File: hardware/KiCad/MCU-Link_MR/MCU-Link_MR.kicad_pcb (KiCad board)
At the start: 2 copper layers, 57.9 x 39.9 mm, 108 parts, among them J1 Pixhawk Debug Full (1x10 JST-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, J11 JST-GH_BM06B, J2 Pixhawk_Debug_Mini (1x06 JST-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, J3 Jumper_2_Open, J4 Jumper_2_Open, J5 Jumper_2_Open, J6 Conn_02x05_Odd_Even, J8 DCD-LZ_Debug (1x07 JST-GHS), J9 USB4110-GF-A_REVB, SW1 KMR221GLFS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

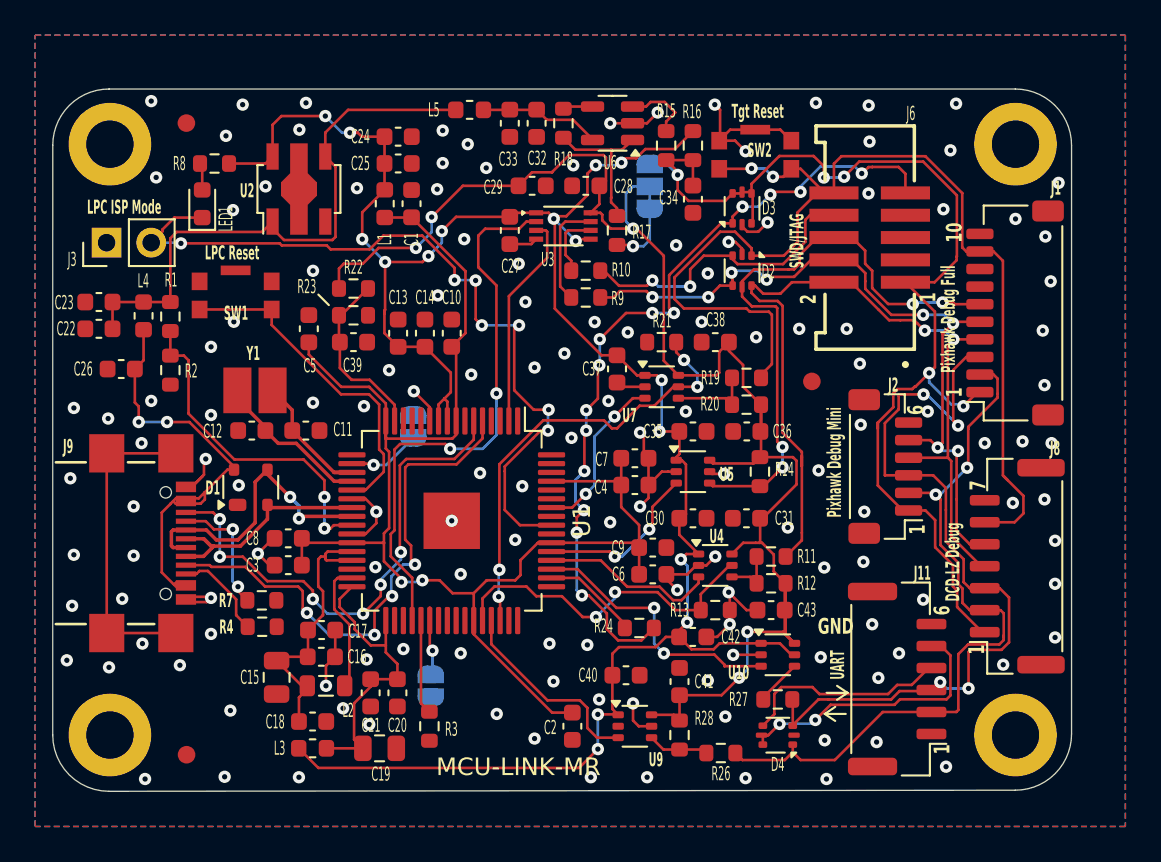
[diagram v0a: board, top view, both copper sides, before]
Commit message: sent v0.2 to PCB production
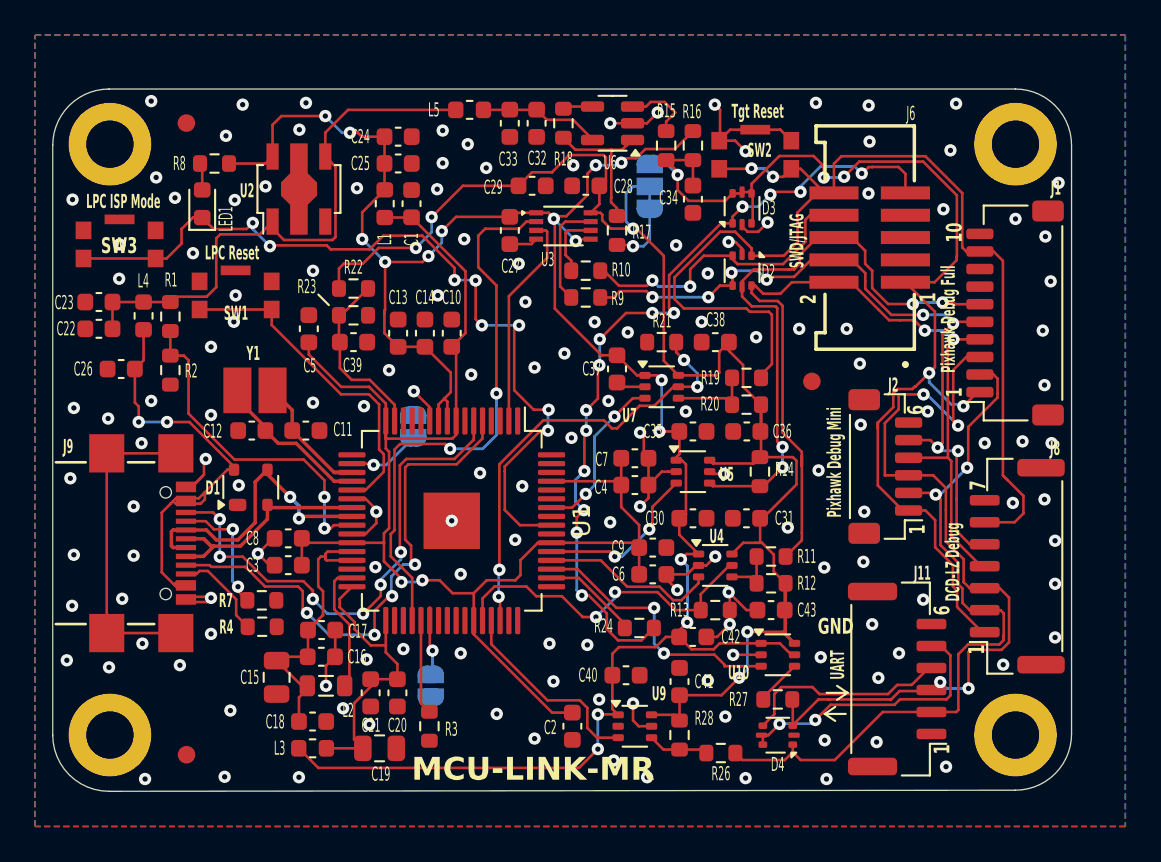
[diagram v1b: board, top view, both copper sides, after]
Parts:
- removed J3: Jumper_2_Open, Connector_PinHeader_2.54mm:PinHeader_1x02_P2.54mm_Vertical
- added SW3: KMR221GLFS, McuOnEclipse:SW_C_K_KMR2, F.Cu at (167.8, 86.9)
- moved L6 1.17 mm to (195.5, 89.8)
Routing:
- net PIO0_5-ISP_EN-LED1_CTRL: track 45.9 -> 48.7 mm, vias 7 -> 8
- net GND: vias 143 -> 149
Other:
- board text added: "V0.2 1-May-2024"
- board text removed: "V0.2 29-Apr-2024"
